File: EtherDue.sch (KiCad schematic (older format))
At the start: 0 parts

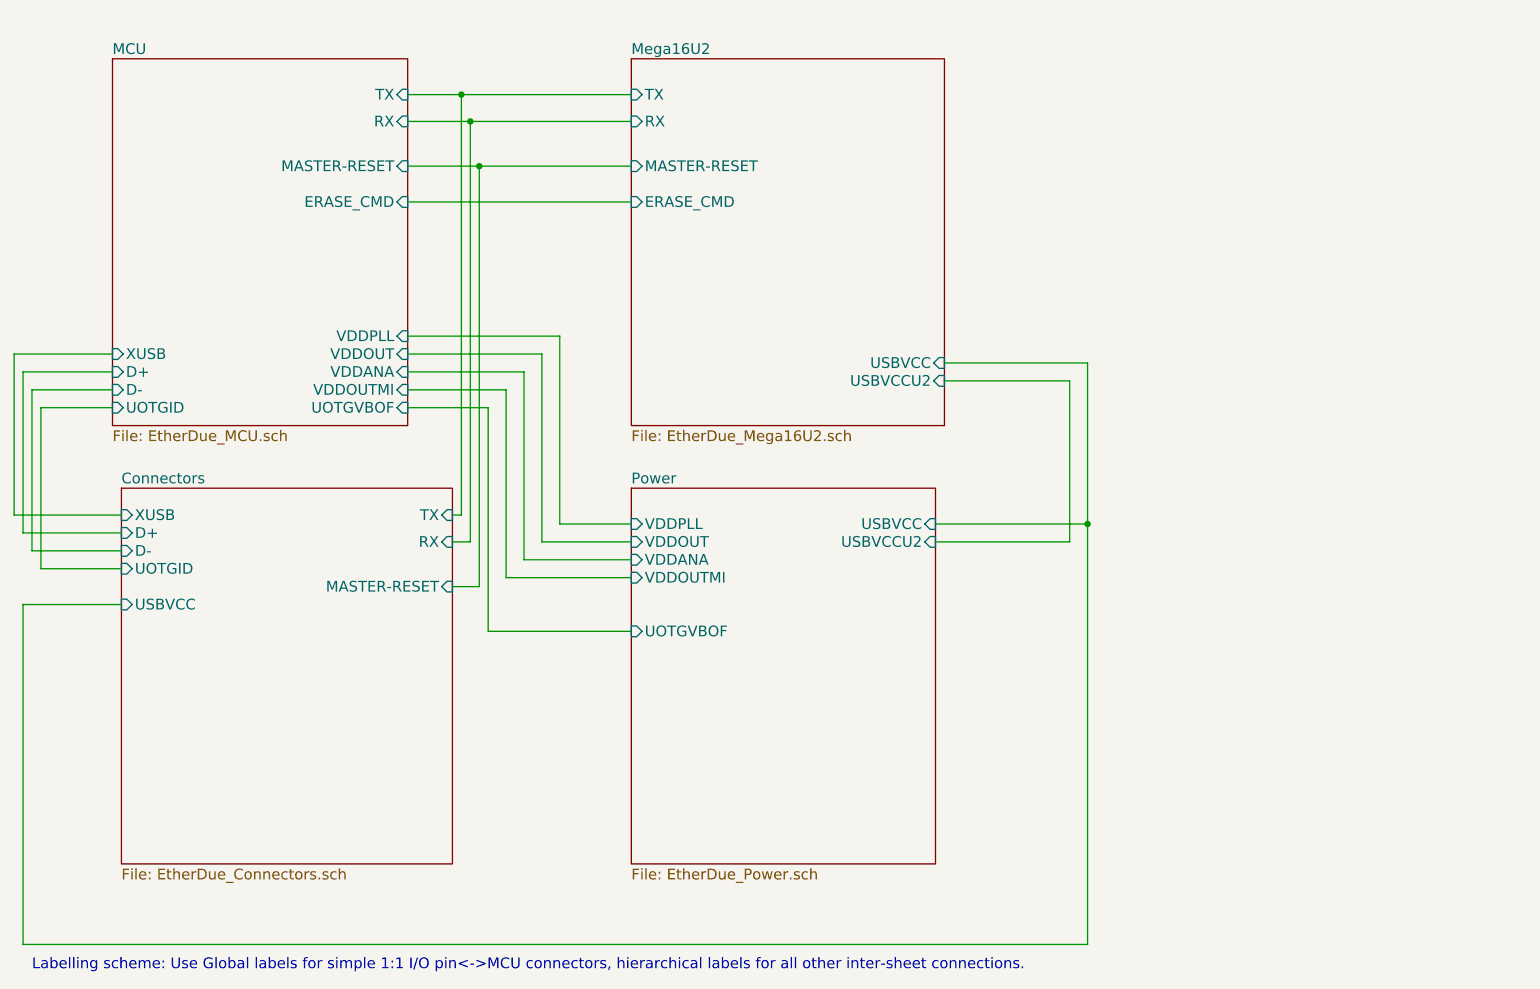
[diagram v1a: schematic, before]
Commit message: Add W5100 Ethernet components
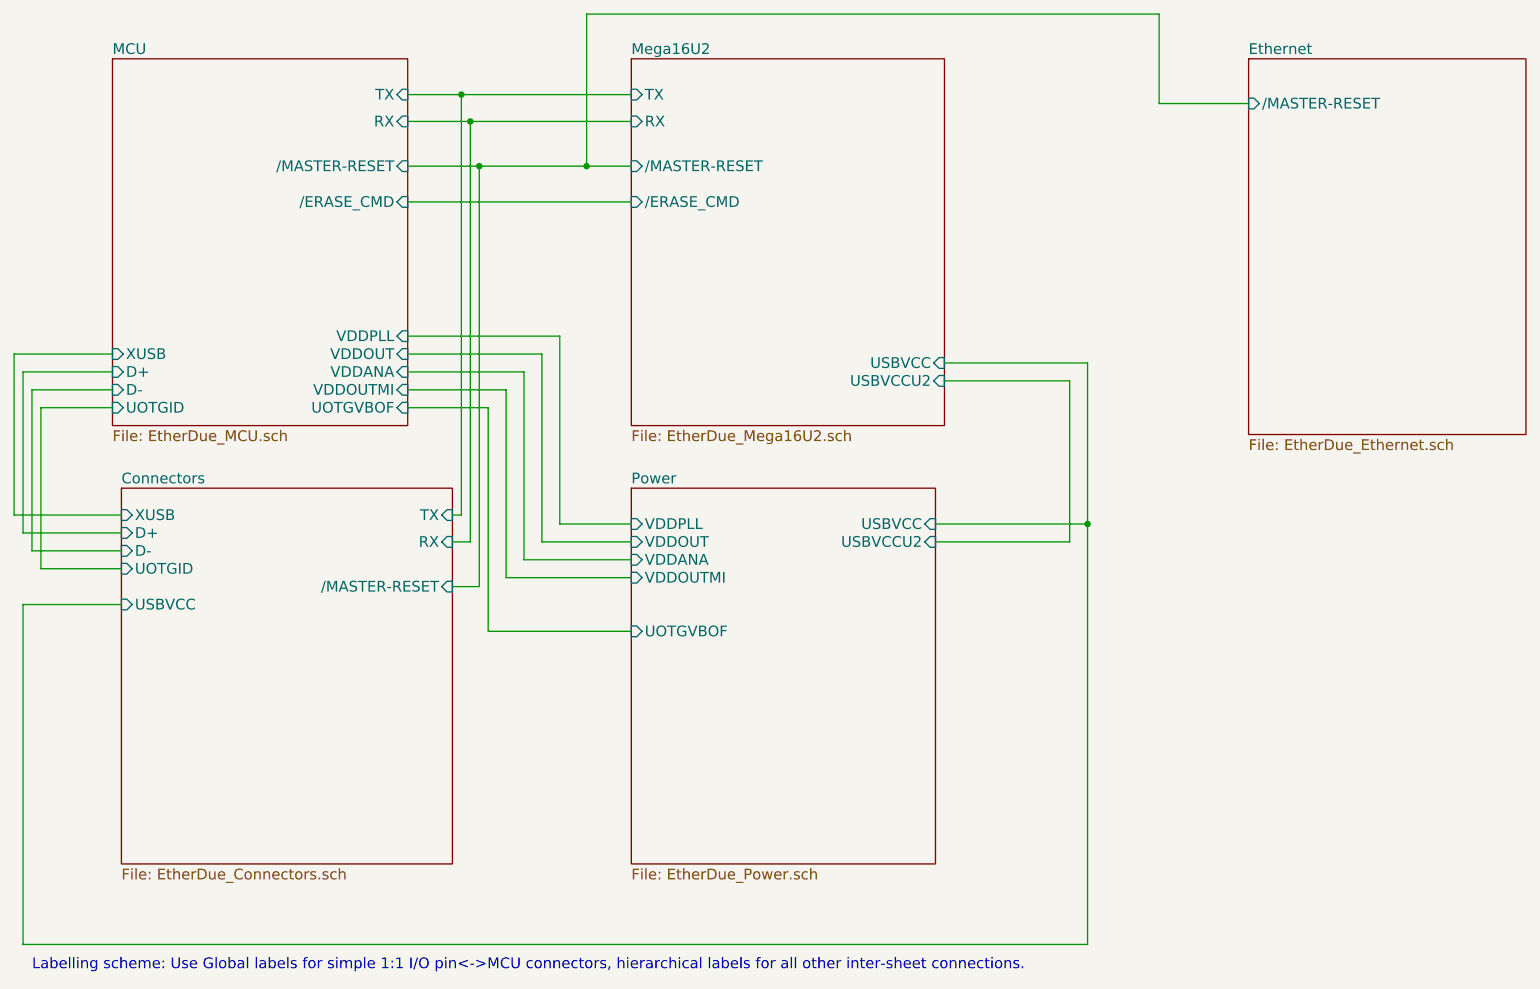
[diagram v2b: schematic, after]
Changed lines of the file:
@@
-EESchema Schematic File Version 2  date Wed 10 Apr 2013 15:09:30 EST
+EESchema Schematic File Version 2  date Thu 11 Apr 2013 15:03:05 EST
 LIBS:power
 LIBS:device
@@
 $Descr A4 11700 8267
 encoding utf-8
-Sheet 1 5
+Sheet 1 6
 Title ""
-Date "10 apr 2013"
+Date "11 apr 2013"
 Rev ""
 Comp ""
@@
 Comment4 ""
 $EndDescr
+Wire Wire Line
+	7450 1300 6950 1300
+Wire Wire Line
+	6950 1300 6950 800
+Wire Wire Line
+	6950 800  3750 800
+Connection ~ 3750 1650
+Wire Wire Line
+	3750 800  3750 1650
+Connection ~ 3100 1400
+Wire Wire Line
+	3000 3750 3100 3750
+Wire Wire Line
+	3100 3750 3100 1400
+Wire Wire Line
+	1100 2700 550  2700
+Wire Wire Line
+	550  2700 550  3600
+Wire Wire Line
+	1100 2900 650  2900
+Wire Wire Line
+	650  2900 650  3800
+Wire Wire Line
+	1150 3900 700  3900
+Connection ~ 6550 3650
+Wire Wire Line
+	6550 6000 6550 2750
+Wire Wire Line
+	6550 6000 600  6000
+Wire Wire Line
+	1150 3700 600  3700
+Wire Wire Line
+	5750 2850 6450 2850
+Wire Wire Line
+	6450 2850 6450 3750
+Wire Wire Line
+	6450 3750 5700 3750
+Wire Wire Line
+	2750 2900 3300 2900
+Wire Wire Line
+	3300 2900 3300 3950
+Wire Wire Line
+	3300 3950 4000 3950
+Wire Wire Line
+	4000 3750 3500 3750
+Wire Wire Line
+	3500 3750 3500 2700
+Wire Wire Line
+	3500 2700 2750 2700
+Wire Wire Line
+	2750 1650 4000 1650
+Wire Wire Line
+	4000 1400 2750 1400
+Wire Wire Line
+	2750 1250 4000 1250
+Wire Wire Line
+	2750 1850 4000 1850
+Wire Wire Line
+	2750 2600 3600 2600
+Wire Wire Line
+	3600 2600 3600 3650
+Wire Wire Line
+	3600 3650 4000 3650
+Wire Wire Line
+	2750 2800 3400 2800
+Wire Wire Line
+	3400 2800 3400 3850
+Wire Wire Line
+	3400 3850 4000 3850
+Wire Wire Line
+	5700 3650 6550 3650
+Wire Wire Line
+	6550 2750 5750 2750
+Wire Wire Line
+	2750 3000 3200 3000
+Wire Wire Line
+	3200 3000 3200 4250
+Wire Wire Line
+	3200 4250 4000 4250
+Wire Wire Line
+	550  3600 1150 3600
+Wire Wire Line
+	650  3800 1150 3800
+Wire Wire Line
+	600  6000 600  4100
+Wire Wire Line
+	600  4100 1150 4100
+Wire Wire Line
+	700  3900 700  3000
+Wire Wire Line
+	700  3000 1100 3000
+Wire Wire Line
+	600  3700 600  2800
+Wire Wire Line
+	600  2800 1100 2800
+Wire Wire Line
+	3000 3600 3050 3600
+Wire Wire Line
+	3050 3600 3050 1250
+Connection ~ 3050 1250
+Wire Wire Line
+	3000 4000 3150 4000
+Wire Wire Line
+	3150 4000 3150 1650
 Connection ~ 3150 1650
-Wire Wire Line
-	3150 1650 3150 4000
-Wire Wire Line
-	3150 4000 3000 4000
-Connection ~ 3050 1250
-Wire Wire Line
-	3050 1250 3050 3600
-Wire Wire Line
-	3050 3600 3000 3600
-Wire Wire Line
-	1100 2800 600  2800
-Wire Wire Line
-	600  2800 600  3700
-Wire Wire Line
-	1100 3000 700  3000
-Wire Wire Line
-	700  3000 700  3900
-Wire Wire Line
-	1150 4100 600  4100
-Wire Wire Line
-	600  4100 600  6000
-Wire Wire Line
-	1150 3800 650  3800
-Wire Wire Line
-	1150 3600 550  3600
-Wire Wire Line
-	4000 4250 3200 4250
-Wire Wire Line
-	3200 4250 3200 3000
-Wire Wire Line
-	3200 3000 2750 3000
-Wire Wire Line
-	5750 2750 6550 2750
-Wire Wire Line
-	5700 3650 6550 3650
-Wire Wire Line
-	4000 3850 3400 3850
-Wire Wire Line
-	3400 3850 3400 2800
-Wire Wire Line
-	3400 2800 2750 2800
-Wire Wire Line
-	4000 3650 3600 3650
-Wire Wire Line
-	3600 3650 3600 2600
-Wire Wire Line
-	3600 2600 2750 2600
-Wire Wire Line
-	2750 1850 4000 1850
-Wire Wire Line
-	2750 1250 4000 1250
-Wire Wire Line
-	4000 1400 2750 1400
-Wire Wire Line
-	2750 1650 4000 1650
-Wire Wire Line
-	2750 2700 3500 2700
-Wire Wire Line
-	3500 2700 3500 3750
-Wire Wire Line
-	3500 3750 4000 3750
-Wire Wire Line
-	4000 3950 3300 3950
-Wire Wire Line
-	3300 3950 3300 2900
-Wire Wire Line
-	3300 2900 2750 2900
-Wire Wire Line
-	5700 3750 6450 3750
-Wire Wire Line
-	6450 3750 6450 2850
-Wire Wire Line
-	6450 2850 5750 2850
-Wire Wire Line
-	600  3700 1150 3700
-Wire Wire Line
-	600  6000 6550 6000
-Wire Wire Line
-	6550 6000 6550 2750
-Connection ~ 6550 3650
-Wire Wire Line
-	700  3900 1150 3900
-Wire Wire Line
-	650  3800 650  2900
-Wire Wire Line
-	650  2900 1100 2900
-Wire Wire Line
-	550  3600 550  2700
-Wire Wire Line
-	550  2700 1100 2700
-Wire Wire Line
-	3100 1400 3100 3750
-Wire Wire Line
-	3100 3750 3000 3750
-Connection ~ 3100 1400
+$Sheet
+S 7450 1050 1550 2100
+U 51651351
+F0 "Ethernet" 60
+F1 "EtherDue_Ethernet.sch" 60
+F2 "/MASTER-RESET" I L 7450 1300 60
+$EndSheet
 $Sheet
 S 1100 1050 1650 2050
@@
 F2 "TX" I R 2750 1250 60
 F3 "RX" I R 2750 1400 60
-F4 "MASTER-RESET" I R 2750 1650 60
-F5 "VDDANA" I R 2750 2800 60
-F6 "VDDOUTMI" I R 2750 2900 60
-F7 "ERASE_CMD" I R 2750 1850 60
-F8 "VDDPLL" I R 2750 2600 60
-F9 "VDDOUT" I R 2750 2700 60
-F10 "UOTGVBOF" I R 2750 3000 60
-F11 "XUSB" I L 1100 2700 60
-F12 "D+" I L 1100 2800 60
-F13 "D-" I L 1100 2900 60
-F14 "UOTGID" I L 1100 3000 60
+F4 "VDDANA" I R 2750 2800 60
+F5 "VDDOUTMI" I R 2750 2900 60
+F6 "/ERASE_CMD" I R 2750 1850 60
+F7 "VDDPLL" I R 2750 2600 60
+F8 "VDDOUT" I R 2750 2700 60
+F9 "UOTGVBOF" I R 2750 3000 60
+F10 "XUSB" I L 1100 2700 60
+F11 "D+" I L 1100 2800 60
+F12 "D-" I L 1100 2900 60
+F13 "UOTGID" I L 1100 3000 60
+F14 "/MASTER-RESET" I R 2750 1650 60
 $EndSheet
 $Sheet
@@
 F5 "USBVCC" I L 1150 4100 60
 F6 "XUSB" I L 1150 3600 60
-F7 "MASTER-RESET" I R 3000 4000 60
+F7 "/MASTER-RESET" I R 3000 4000 60
 F8 "RX" I R 3000 3750 60
 F9 "TX" I R 3000 3600 60
@@
 F3 "RX" I L 4000 1400 60
 F4 "USBVCC" I R 5750 2750 60
-F5 "ERASE_CMD" I L 4000 1850 60
-F6 "MASTER-RESET" I L 4000 1650 60
+F5 "/ERASE_CMD" I L 4000 1850 60
+F6 "/MASTER-RESET" I L 4000 1650 60
 F7 "USBVCCU2" I R 5750 2850 60
 $EndSheet
